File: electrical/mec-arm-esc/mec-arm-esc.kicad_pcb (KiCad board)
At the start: 4 copper layers, 60 x 60 mm, 179 parts, among them J1 GT-A1257WRS-103SBT01, J2 BM04B-GHS-TBT, J3 SM05B-GHS-TB, J4 S10B-PHDSS, J5 XY-SM02B-GHS-TB, J6 Header_2Rows-05Pins, J7 Conn_02x01, J8 Conn_01x04, J9 XT30PW-M, Q1 STL110N10F7, Q2 STL110N10F7, Q3 STL110N10F7, Q4 STL110N10F7, Q5 STL110N10F7, Q6 STL110N10F7, Q8 PJA138K_R1_00001, Q9 TJ60S04M3L-VB, SW1 SH-1808SN-250GF, SW2 SH-1808SN-250GF, U1 TCAN330DCNT, U2 STM32G474RET3, U3 DRV8323SRTAT, U4 ESD2CAN24DBZRQ1, U5 AS5047P-ATSM_C22459881, U6 TPS2116DRLR, U7 LMR51625XDDCR_C44750835, U8 AP7366EA-33W5-7, X1 3225 8M 12PF 10PPM

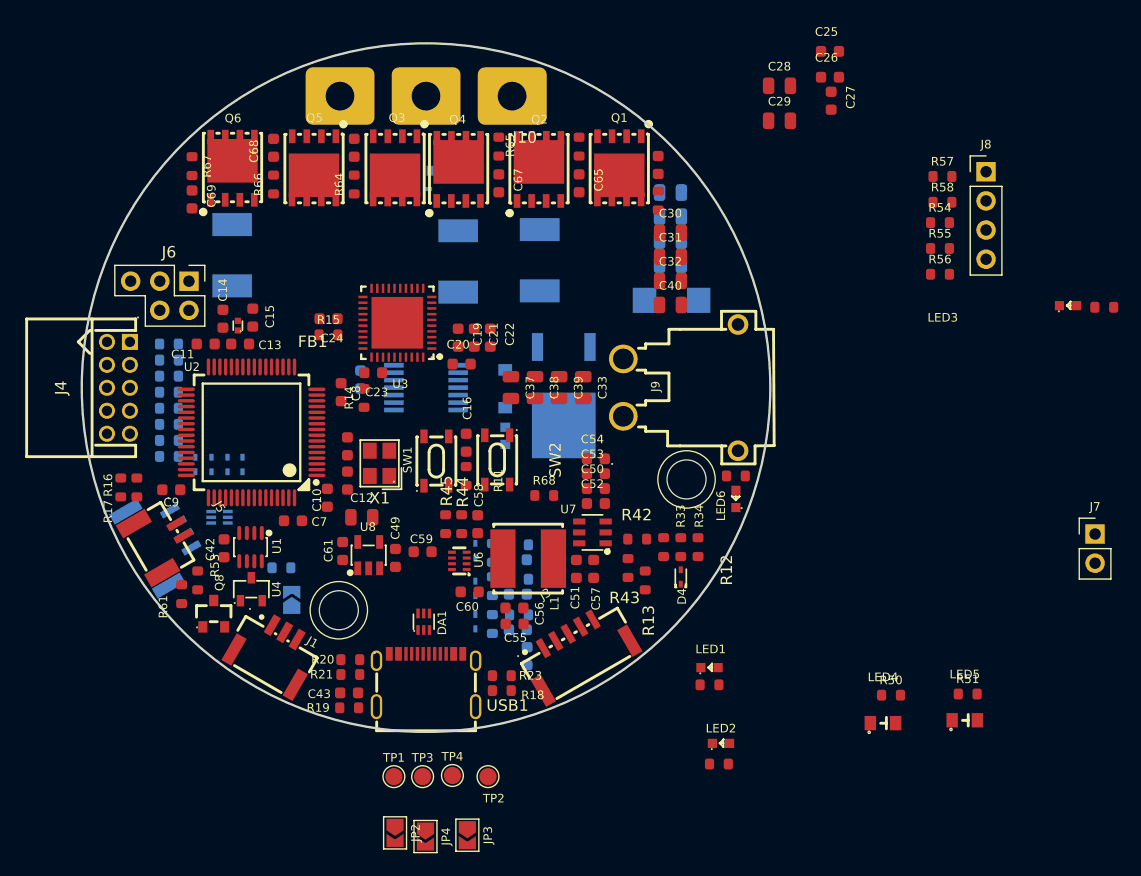
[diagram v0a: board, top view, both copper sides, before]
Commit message: All signal routing finishes, power and planes not yet
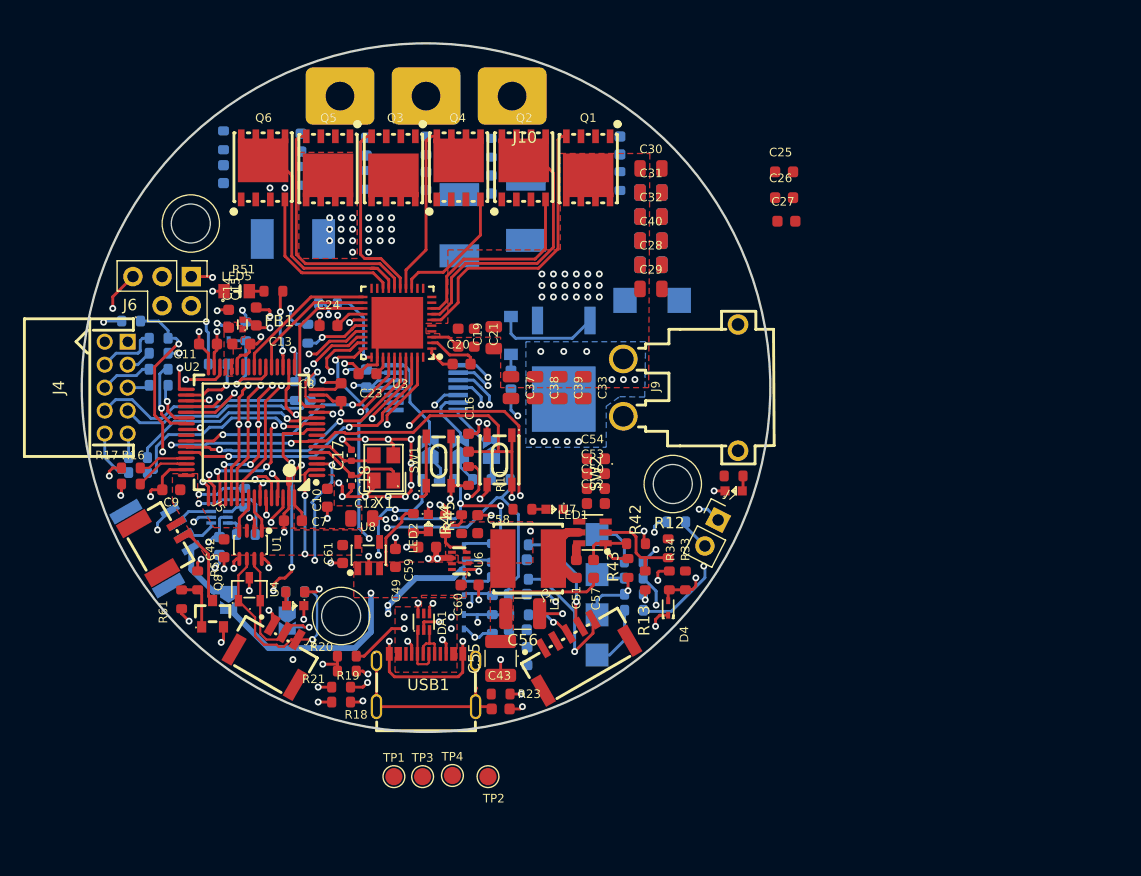
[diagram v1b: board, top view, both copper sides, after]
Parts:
- removed D6, D7, D8, D9: BAT30KFILM, core:SOD-523_L1.2-W0.8-LS1.6-RD-1
- removed LED4: LTST-C171KGKT, core:LED0805-RD
- added C62: 0.1uF, core:C_0603, B.Cu at (132.0, 113.8)
- added JP5: SolderJumper_2_Open, Jumper:SolderJumper-2_P1.3mm_Open_TrianglePad1.0x1.5mm, B.Cu at (132.8, 118.5)
- added NT1: NetTie_2, NetTie:NetTie-2_SMD_Pad0.5mm, F.Cu at (138.1, 107.9)
- added R60: 1k, core:R_0603, B.Cu at (171.8, 111.7)
- added R69: 1k, core:R_0603, B.Cu at (134.2, 109.6)
- added R70: 1.8k, core:R_0603, B.Cu at (156.5, 108.0)
- added R71: 1.8k, core:R_0603, B.Cu at (153.2, 108.0)
- added R72: 1.8k, core:R_0603, B.Cu at (150.4, 108.0)
- C17, C18: footprint core:C_0603 -> Capacitor_SMD:C_0402_1005Metric
- C22: footprint core:C_0603 -> core:C_0805
- C23: value 1uF -> 1uF 6.3V
- C43: value 1nF -> 10nF
- C55, C56: footprint core:C_0603 -> Capacitor_SMD:C_1210_3225Metric
- C64, C65, C66, C67, C68, C69, JP2, JP3, JP4, R14, R15, R50, R54, R55, R56, R57, R58, R62, R63, R64, R65, R66, R67: moved to B.Cu
- J8: value Conn_01x04 -> ~; footprint Connector_PinHeader_2.54mm:PinHeader_1x04_P2.54mm_Vertical -> my_connector:TestPadArray1x4; moved to B.Cu
- R23: value 1M -> 2.55M
- R24: footprint core:R0603 -> core:R_0603
- R34: value 6.38k -> 6.34k
- R35: value 10.24k -> 3.24k
- R42: value 100k -> 100k 0.5%
- R43: value 19.1k -> 19.1k 0.5%
- R45: value 40k -> 40.2k
- R68: value 0 -> 1k; moved to B.Cu
- moved R49 74.7 mm to (138.6, 117.8)
- moved R50 73.8 mm to (124.3, 94.2)
- moved LED5 73.6 mm to (133.5, 91.6)
- moved LED3 72.2 mm to (138.6, 119.0), turned to 180 degrees
- moved R51 69.9 mm to (136.7, 91.6)
- moved R54 64.1 mm to (131.8, 98.0), turned to 180 degrees
- moved J8 53.1 mm to (161.9, 119.4), turned to 90 degrees
- moved R57 44.1 mm to (168.1, 116.6)
- moved R58 41.3 mm to (168.1, 115.2)
- moved R55 41.3 mm to (168.1, 119.4)
- moved R56 38.6 mm to (168.1, 118.0)
- moved JP4 34.2 mm to (155.7, 105.4), turned to 90 degrees
- moved R48 33.9 mm to (148.9, 111.8), turned to 90 degrees
- moved JP3 33.6 mm to (153.0, 105.4), turned to 90 degrees
- moved JP2 33.5 mm to (150.3, 105.4), turned to 90 degrees
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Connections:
- net /peripherals/EXT_FORCE1+ renamed /peripherals/EXT_FORCE1
- net /peripherals/EXT_FORCE1- renamed /peripherals/EXT_FORCE2
- net /peripherals/EXT_FORCE2+ renamed /peripherals/EXT_FORCE3
- net /peripherals/EXT_FORCE2- renamed /peripherals/EXT_FORCE4
- net ADC_FORCE2+ renamed ADC_FORCE3
- net ADC_FORCE2- renamed ADC_FORCE4
- net Net-(DA1-I/O1-Pad6) renamed /peripherals/USB_D_O_N
- net Net-(DA1-I/O2-Pad4) renamed /peripherals/USB_D_O_P
- C17 pad 2: GND -> OSC_GND
- C18 pad 2: GND -> OSC_GND
- C21 pad 2: PGND -> GND
- C22 pad 2: PGND -> GND
- C25 pad 2: PGND -> GND
- C26 pad 2: PGND -> GND
- C27 pad 2: PGND -> GND
- C28 pad 2: PGND -> GND
- C29 pad 2: PGND -> GND
- C30 pad 2: PGND -> GND
- C31 pad 2: PGND -> GND
- C32 pad 2: PGND -> GND
- C33 pad 2: PGND -> GND
- C34 pad 2: PGND -> GND
- C35 pad 2: PGND -> GND
- C36 pad 2: PGND -> GND
- C37 pad 2: PGND -> GND
- C38 pad 2: PGND -> GND
- C39 pad 2: PGND -> GND
- C40 pad 2: PGND -> GND
- C41 pad 2: PGND -> GND
- C49 pad 2: PGND -> GND
- C50 pad 1: PGND -> GND
- C52 pad 1: PGND -> GND
- C53 pad 1: PGND -> GND
- C54 pad 1: PGND -> GND
- C55 pad 1: PGND -> GND
- C56 pad 1: PGND -> GND
- C58 pad 1: PGND -> GND
- C59 pad 2: PGND -> GND
- C60 pad 2: PGND -> GND
- C61 pad 2: PGND -> GND
- D11 pad 2: PGND -> GND
- DA2 pad 4: UART_TX -> Net-(DA2-I/O2-Pad4)
- DA2 pad 5: +5V_ESC -> +3V3
- DA2 pad 6: UART_RX -> Net-(DA2-I/O1-Pad6)
- J2 pad 4: +5V_ESC -> Net-(JP5-A)
- J3 pad 3: ENC_Z -> /peripherals/ENC_Z_IN
- J3 pad 4: ENC_B -> /peripherals/ENC_B_IN
- J3 pad 5: ENC_A -> /peripherals/ENC_A_IN
- J4 pad 1: PGND -> GND
- J4 pad 2: +5V_ESC -> +3V3
- J4 pad 5: /peripherals/GPIO_CTRL2 -> /peripherals/GPIO_CTRL1
- J4 pad 6: /peripherals/GPIO_CTRL1 -> /peripherals/GPIO_CTRL2
- J7 pad 2: DAC_OUT1 -> Net-(J7-Pin_2)
- J9 pad 1: PGND -> GND
- JP1 pad 2: /peripherals/CAN_N -> /peripherals/CAN_P
- JP2 pad 1: ENC_Z -> Net-(JP2-A)
- JP3 pad 1: ENC_B -> Net-(JP3-A)
- JP4 pad 1: ENC_A -> Net-(JP4-A)
- LED1 pad 1: PGND -> GND
- LED2 pad 1: PGND -> GND
- LED3 pad 1: PGND -> GND
- LED6 pad 1: PGND -> GND
- Q8 pad 2: PGND -> GND
- R1 pad 1: PGND -> GND
- R13 pad 1: PGND -> GND
- R2 pad 1: PGND -> GND
- R22 pad 1: Net-(JP1-A) -> /peripherals/CAN_N
- R22 pad 2: /peripherals/CAN_P -> Net-(JP1-A)
- R24 pad 1: PGND -> GND
- R27 pad 1: ENC_A -> /peripherals/ENC_A_IN
- R28 pad 1: ENC_B -> /peripherals/ENC_B_IN
- R29 pad 1: ENC_Z -> /peripherals/ENC_Z_IN
- R3 pad 1: PGND -> GND
- R34 pad 1: PGND -> GND
- R36 pad 1: ADC_FORCE1+ -> ADC_FORCE1
- R39 pad 2: ADC_FORCE1- -> ADC_FORCE2
- R40 pad 1: GPIO_EXT1 -> GPIO_EXT2
- R40 pad 2: /peripherals/GPIO_CTRL1 -> /peripherals/GPIO_CTRL2
- R41 pad 1: /peripherals/GPIO_CTRL2 -> /peripherals/GPIO_CTRL1
- R41 pad 2: GPIO_EXT2 -> GPIO_EXT1
- R43 pad 1: PGND -> GND
- R45 pad 1: PGND -> GND
- R50 pad 1: Net-(LED4-A) -> GND
- R50 pad 2: LED_DEBUG1 -> LASER_CTRL
- R68 pad 1: GND -> UART_RX
- R68 pad 2: PGND -> Net-(DA2-I/O1-Pad6)
- U2 pad 14: ADC_FORCE1+ -> ADC_FORCE2
- U2 pad 17: ADC_FORCE1- -> ADC_FORCE1
- U2 pad 19: LED_DEBUG2 -> LED_DEBUG1
- U2 pad 8: LED_DEBUG1 -> unconnected-(U2-PC0-Pad8)
- U3 pad 10: PGND -> GND
- U3 pad 11: PGND -> GND
- U3 pad 20: PGND -> GND
- U3 pad 40: PGND -> GND
- U3 pad 41: PGND -> GND
- U6 pad 1: PGND -> GND
- U7 pad 4: PGND -> GND
- U8 pad 2: PGND -> GND
- X1 pad 2: GND -> OSC_GND
- X1 pad 4: GND -> OSC_GND
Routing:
- net GND: track 0.00 -> 120.4 mm, vias 0 -> 61
- net +3V3: track 0.00 -> 67.6 mm, vias 0 -> 18
- net DAC_OUT1: track 0.00 -> 59.2 mm, vias 0 -> 2
- net NRST: track 0.00 -> 57.7 mm, vias 0 -> 3
- net SPI_MISO: track 0.00 -> 55.5 mm, vias 0 -> 4
- net SPI_SCK: track 0.00 -> 49.9 mm, vias 0 -> 6
- net VBUS_SENSE: track 0.00 -> 49.8 mm, vias 0 -> 4
- net SPI_MOSI: track 0.00 -> 49.6 mm, vias 0 -> 4
- net ENC_Z: track 0.00 -> 43.6 mm, vias 0 -> 4
- net LASER_CTRL: track 0.00 -> 40.8 mm, vias 0 -> 4
- net ENC_A: track 0.00 -> 40.3 mm, vias 0 -> 3
- net ENC_B: track 0.00 -> 38.9 mm, vias 0 -> 4
- net SPI_ENC_CS: track 0.00 -> 36.9 mm, vias 0 -> 4
- net /peripherals/USB_D_O_N: track 0.00 -> 35.7 mm, vias 0 -> 2
- net /peripherals/USB_D_O_P: track 0.00 -> 33.7 mm, vias 0 -> 2
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- added copper zone on F.Cu, net +3V3
- added copper zone on F.Cu, net +3V3A
- added copper zone on F.Cu, net +5V_ESC
- added copper zone on F.Cu, net +5V_INT
- added copper zone on F.Cu, net +5V_USB
- added copper zone on In2.Cu, net +5V_USB
- added copper zone on In1.Cu, net OSC_GND
- added copper zone on B.Cu, net PWR_IN
- added copper zone on In2.Cu, net PWR_IN
- added copper zone on F.Cu, net VBUS
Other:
- outline, holes or cut-outs redrawn

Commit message: Completed ESC PCB
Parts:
- removed JP2: SolderJumper_2_Open, Jumper:SolderJumper-2_P1.3mm_Open_TrianglePad1.0x1.5mm
- removed R72: 1.8k, core:R_0603
- removed TP1, TP2, TP3, TP4: ~, TestPoint:TestPoint_Pad_D1.5mm
- added G***: LOGO, LOGO, F.Cu at (170.5, 82.9)
- added G***: LOGO, LOGO, F.Cu at (130.9, 79.0)
- added G***: LOGO, LOGO, F.Cu at (136.9, 87.8)
- added G***: LOGO, LOGO, B.Cu at (150.0, 126.0)
- added G***: LOGO, LOGO, B.Cu at (150.1, 93.7)
- added G***: LOGO, LOGO, B.Cu at (145.5, 114.0)
- added J11: XT30PW-M, my_connector:CONN-TH_XT30PW-M, F.Cu at (172.5, 100.0)
- added J12: ~, my_connector:3x3BusBar Pad, F.Cu at (164.1, 86.7)
- C26, C27, C33: moved to B.Cu
- C35, C36: moved to F.Cu
- J9: value XT30PW-M -> ~; footprint my_connector:CONN-TH_XT30PW-M -> my_connector:5x3BusBar Pad
- moved R60 53.0 mm to (124.8, 87.2), turned to -90 degrees
- moved J7 52.2 mm to (129.5, 86.7), turned to -90 degrees
- moved C26 37.9 mm to (143.3, 84.2), turned to -90 degrees
- moved C27 36.0 mm to (145.4, 84.2), turned to -90 degrees
- moved J9 32.3 mm to (142.8, 86.7), turned to 0 degrees
- moved C30 21.7 mm to (159.6, 100.1)
- moved D10 20.2 mm to (177.4, 98.5)
- moved R24 20.2 mm to (177.4, 102.3)
- moved C37 18.7 mm to (173.6, 90.7), turned to 0 degrees
- moved C38 18.1 mm to (173.6, 88.6), turned to 0 degrees
- moved C39 18.1 mm to (173.6, 86.5), turned to 0 degrees
- moved C31 18.1 mm to (159.6, 98.0)
- moved C36 16.4 mm to (159.6, 95.9)
- moved C32 16.1 mm to (163.8, 100.1), turned to 180 degrees
- moved C25 13.5 mm to (167.8, 82.7), turned to 90 degrees
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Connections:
- C62 pad 2: +3V3 -> +5V_ESC
- DA2 pad 5: +3V3 -> +5V_ESC
- J9 pad 1: GND -> VBUS
- JP3 pad 2: /peripherals/MAG_B -> /peripherals/MAG_A
- JP4 pad 2: /peripherals/MAG_A -> /peripherals/MAG_B
- R70 pad 1: ENC_A -> ENC_B
- R71 pad 1: ENC_B -> ENC_A
- U5 pad 14: /peripherals/MAG_Z -> unconnected-(U5-I/PWM-Pad14)
- U6 pad 8: Net-(U6-ST) -> unconnected-(U6-ST-Pad8)
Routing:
- net VBUS: track 16.9 -> 88.3 mm, vias 39 -> 42
- net GND: track 120.4 -> 185.3 mm, vias 61 -> 100
- net +5V_ESC: track 23.8 -> 78.6 mm, vias 1 -> 3
- net +3V3: track 67.6 -> 119.2 mm, vias 18 -> 25
- net DAC_OUT1: track 59.2 -> 22.8 mm, vias 2 -> 3
- net TEMP_SENSE: track 9.20 -> 29.3 mm
- net /powerstage/SPA: track 0.00 -> 15.0 mm, vias 0 -> 11
- net /powerstage/SPC: track 0.00 -> 14.9 mm, vias 2 -> 11
- net Net-(D10-A): track 1.38 -> 14.0 mm
- net ENC_Z: track 43.6 -> 33.3 mm, vias 4 -> 3
- net PHASE_B: track 14.7 -> 23.6 mm, vias 0 -> 12
- net /peripherals/MAG_Z: track 8.73 -> 0.00 mm
- net /powerstage/SPB: track 0.00 -> 8.57 mm, vias 0 -> 11
- net Net-(U3-CAL): track 6.95 -> 2.39 mm
- net Net-(JP2-A): track 2.58 -> 0.00 mm
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- added copper zone on B.Cu, net +3V3
- added copper zone on In2.Cu, net +3V3
- added copper zone on B.Cu, net /powerstage/SPA
- added copper zone on F.Cu, net /powerstage/SPA
- added copper zone on B.Cu, net /powerstage/SPB
- added copper zone on F.Cu, net /powerstage/SPB
- added copper zone on B.Cu, net /powerstage/SPC
- added copper zone on F.Cu, net /powerstage/SPC
- added copper zone on B.Cu, net GND
- added copper zone on F.Cu, net GND
- added copper zone on In1.Cu, net GND
- added copper zone on In2.Cu, net GND
- added copper zone on B.Cu, net PHASE_A
- added copper zone on F.Cu, net PHASE_A
- added copper zone on B.Cu, net PHASE_B
- added copper zone on F.Cu, net PHASE_B
- added copper zone on B.Cu, net PHASE_C
- added copper zone on F.Cu, net PHASE_C
- added copper zone on F.Cu, net PWR_IN
- added copper zone on B.Cu, net VBUS
- added copper zone on In2.Cu, net VBUS
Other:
- outline, holes or cut-outs redrawn
- board text added: "+"
- board text added: "-"
- board text added: "24V"
- board text added: "3V3"
- board text added: "5V"
- board text added: "A"
- board text added: "ARM 2026"
- board text added: "B"
- board text added: "BOOT"
- board text added: "C"
- board text added: "CAN TERM"
- board text added: "DBG"
- board text added: "GND"
- board text added: "James D."
- board text added: "M E C"
- board text added: "MAG A"
- board text added: "MAG B"
- board text added: "NRST"
- board text added: "RST"
- board text added: "SWDCLK"
- board text added: "SWDIO"
- board text added: "V.1.0"
